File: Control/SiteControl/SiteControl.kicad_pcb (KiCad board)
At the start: 2 copper layers, 109.2 x 48.3 mm, 209 parts, among them J1 RJ50, J2 CONN_01X03, J3 CONN_02X07, J4 CONN_01X06, J5 RS232-Jack, J6 CONN_01X02, J7 USB_A, Q1 BC817-40, Q2 Q_PJFET_GSD, U1 Opto_H11L1M, U10 SS_Relay_VO14642AT, U11 MAX17552, U12 ICL3221, U13 Opto_H11L1M, U14 Opto_H11L1M, U15 12-Bit SPI ADC, U2 Opto_H11L1M, U3 Opto_H11L1M, U4 Opto_H11L1M, U5 Opto_H11L1M, U6 PIC16LF1947, U7 SS_Relay_VO14642AT, U8 SS_Relay_VO14642AT, U9 MC34063, Y1 4MHz

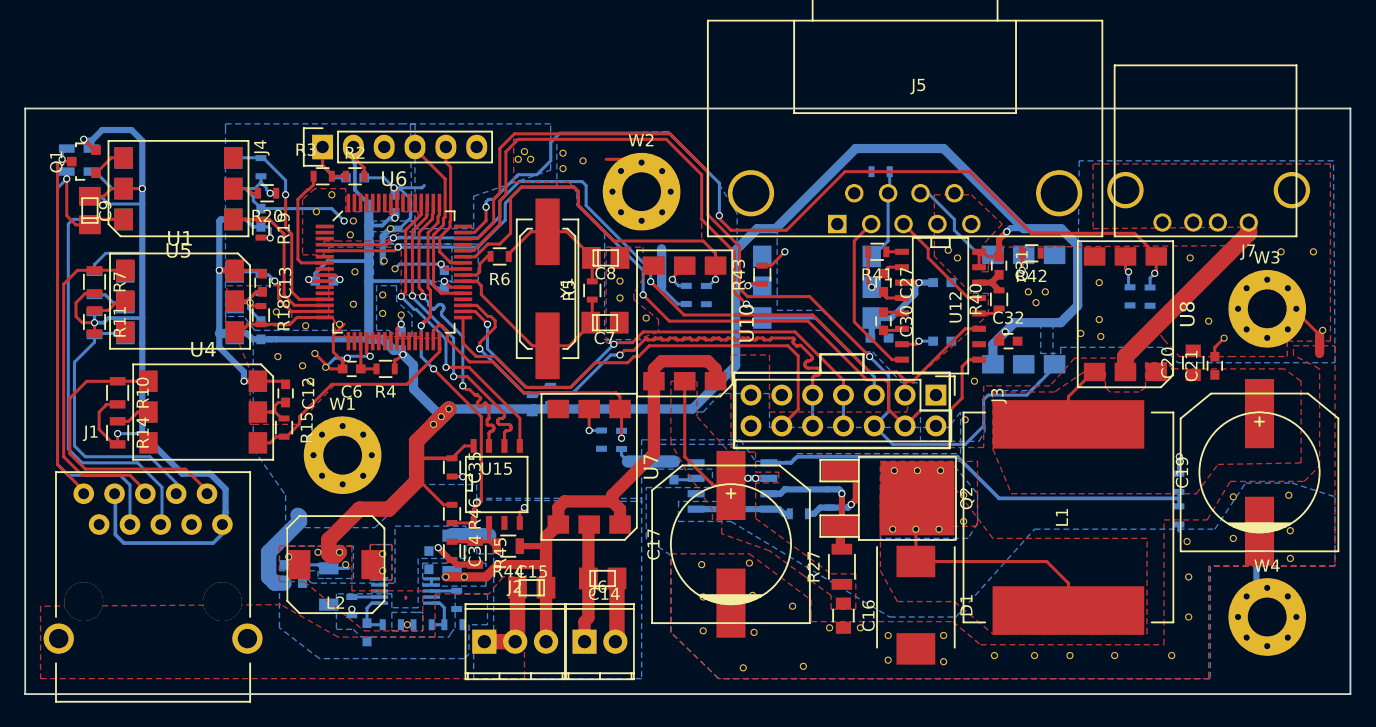
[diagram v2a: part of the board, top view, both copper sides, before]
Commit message: [Changed] Moved the silkscreen identifies as well as added relevant silkscreen text to the board - it should be good to submit to the fab
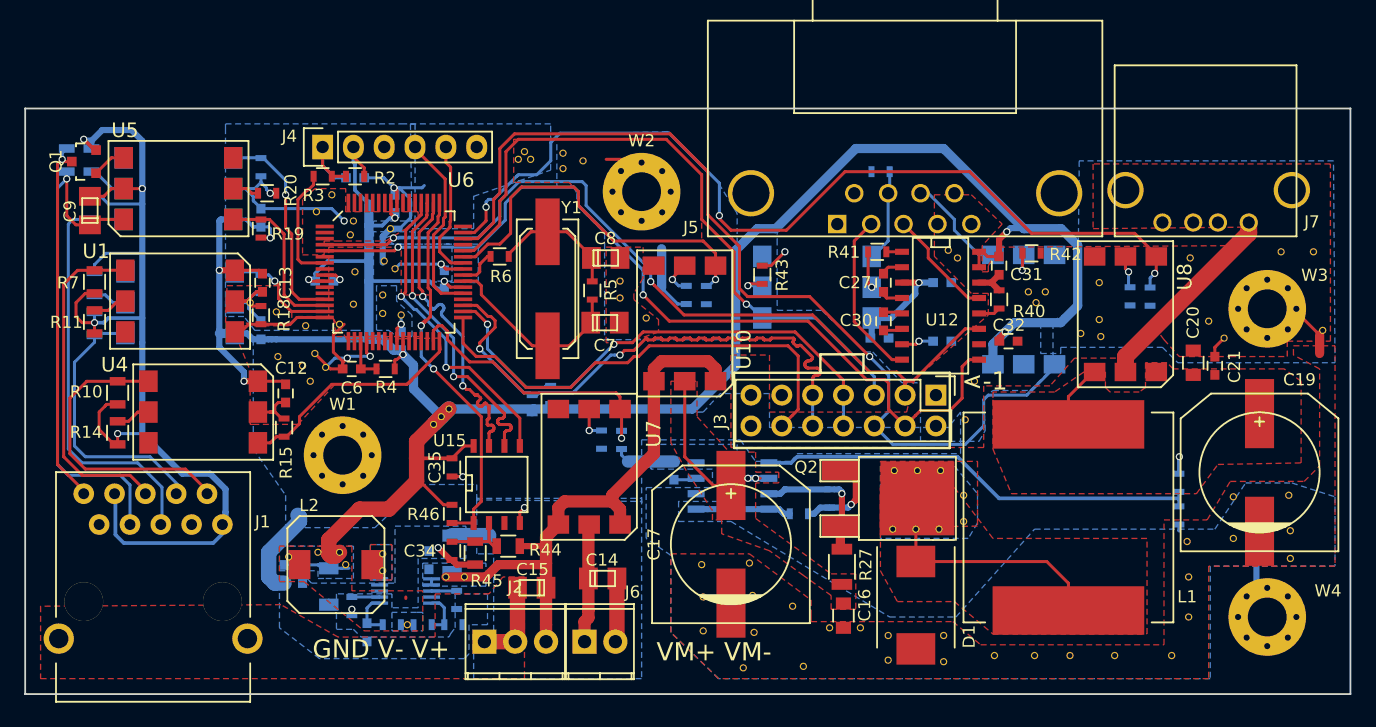
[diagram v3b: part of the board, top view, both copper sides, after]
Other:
- board text added: "<-1"
- board text added: "Applied Physics Club PSU Array Base Control Rev 1.0 The Pennsylvania State University"
- board text added: "GND V- V+"
- board text added: "VM+ VM-"

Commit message: [Added] Site control BOM
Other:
- board text added: "Applied Physics Club PSU Array Site Control Rev 1.0 The Pennsylvania State University"
- board text removed: "Applied Physics Club PSU Array Base Control Rev 1.0 The Pennsylvania State University"
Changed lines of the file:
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@@
     (links 365)
     (no_connects 2)
-    (area 86.284999 63.424999 195.655001 111.835001)
+    (area 85.137535 40.48 214.86 113.305001)
     (thickness 1.6)
     (drawings 19)
@@
     (visible_elements 7FFFFFFF)
     (pcbplotparams
-      (layerselection 0x00030_80000001)
+      (layerselection 0x010f0_80000001)
       (usegerberextensions false)
       (excludeedgelayer true)
@@
       (outputformat 1)
       (mirror false)
-      (drillshape 1)
+      (drillshape 0)
       (scaleselection 1)
       (outputdirectory ""))
@@
     )
   )
-  (gr_text "Applied Physics Club\nPSU Array Base Control Rev 1.0\nThe Pennsylvania State University" (at 163.27 104.17) (layer B.SilkS)
+  (gr_text "Applied Physics Club\nPSU Array Site Control Rev 1.0\nThe Pennsylvania State University" (at 163.27 104.17) (layer B.SilkS)
     (effects (font (size 1.5 1.5) (thickness 0.3)) (justify mirror))
   )
@@
   (gr_line (start 144.78 91.482776) (end 162.56 91.482776) (layer F.SilkS) (width 0.2))
   (dimension 48.26 (width 0.3) (layer Dwgs.User)
-    (gr_text "1.9000 in" (at 208.36 87.63 90) (layer Dwgs.User)
+    (gr_text "48.260 mm" (at 208.36 87.63 90) (layer Dwgs.User)
       (effects (font (size 1.5 1.5) (thickness 0.3)))
     )
@@
     (arrow2b (pts (xy 207.01 111.76) (xy 206.423579 110.633496)))
   )
-  (dimension 109.22 (width 0.3) (layer Dwgs.User)
-    (gr_text "4.3000 in" (at 140.97 41.83) (layer Dwgs.User)
+  (dimension 109.474 (width 0.3) (layer Dwgs.User)
+    (gr_text "109.474 mm" (at 140.839891 41.83) (layer Dwgs.User)
       (effects (font (size 1.5 1.5) (thickness 0.3)))
     )
-    (feature1 (pts (xy 195.58 63.5) (xy 195.58 40.48)))
-    (feature2 (pts (xy 86.36 63.5) (xy 86.36 40.48)))
-    (crossbar (pts (xy 86.36 43.18) (xy 195.58 43.18)))
-    (arrow1a (pts (xy 195.58 43.18) (xy 194.453496 43.766421)))
-    (arrow1b (pts (xy 195.58 43.18) (xy 194.453496 42.593579)))
-    (arrow2a (pts (xy 86.36 43.18) (xy 87.486504 43.766421)))
-    (arrow2b (pts (xy 86.36 43.18) (xy 87.486504 42.593579)))
+    (feature1 (pts (xy 195.576891 63.5) (xy 195.576891 40.48)))
+    (feature2 (pts (xy 86.102891 63.5) (xy 86.102891 40.48)))
+    (crossbar (pts (xy 86.102891 43.18) (xy 195.576891 43.18)))
+    (arrow1a (pts (xy 195.576891 43.18) (xy 194.450387 43.766421)))
+    (arrow1b (pts (xy 195.576891 43.18) (xy 194.450387 42.593579)))
+    (arrow2a (pts (xy 86.102891 43.18) (xy 87.229395 43.766421)))
+    (arrow2b (pts (xy 86.102891 43.18) (xy 87.229395 42.593579)))
   )
   (gr_line (start 86.36 63.5) (end 86.36 111.76) (layer Edge.Cuts) (width 0.15))

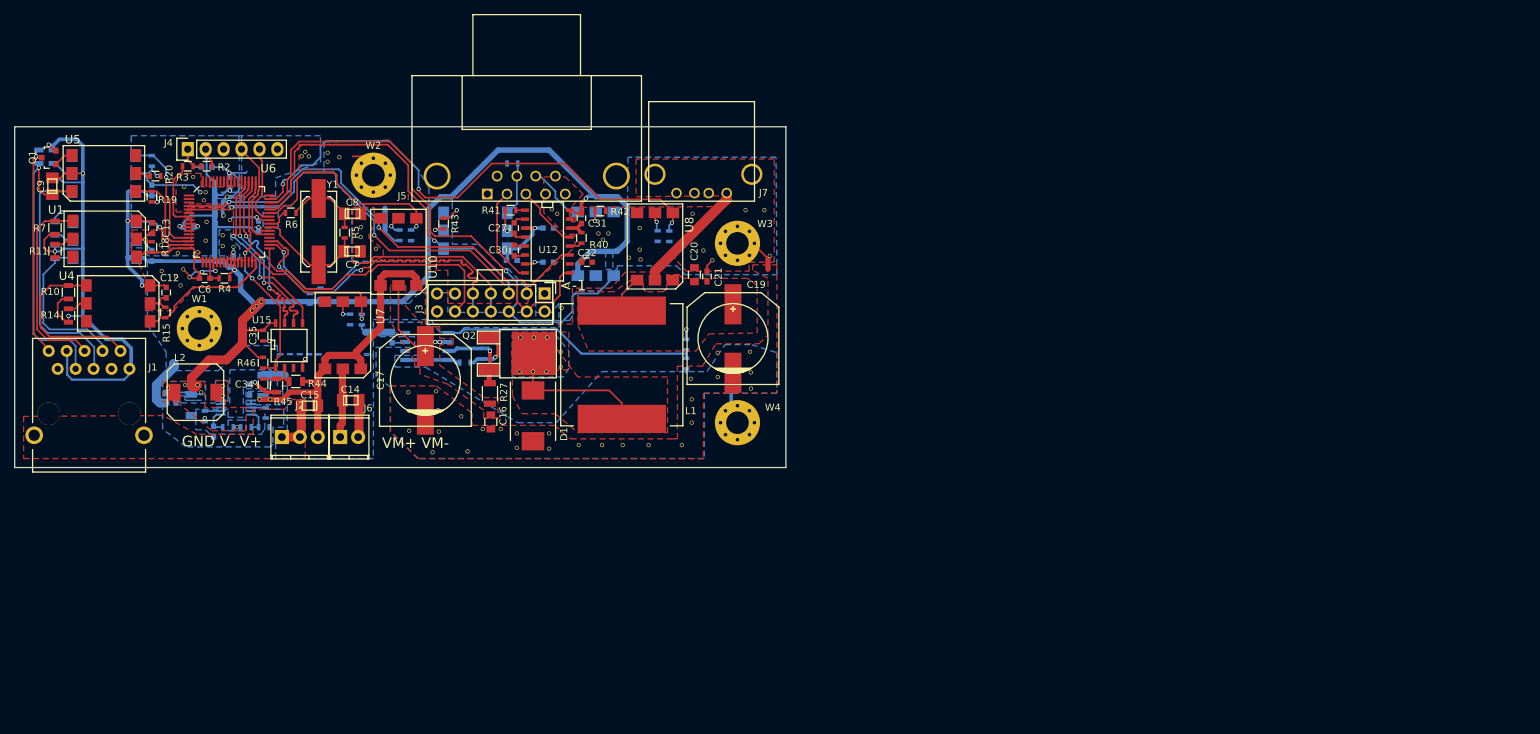
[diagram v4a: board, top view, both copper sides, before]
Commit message: [Added] more parts; [Updated] Site Control board schematic to Rev B; [WIP] Site Control board pcb layout for Rev B.
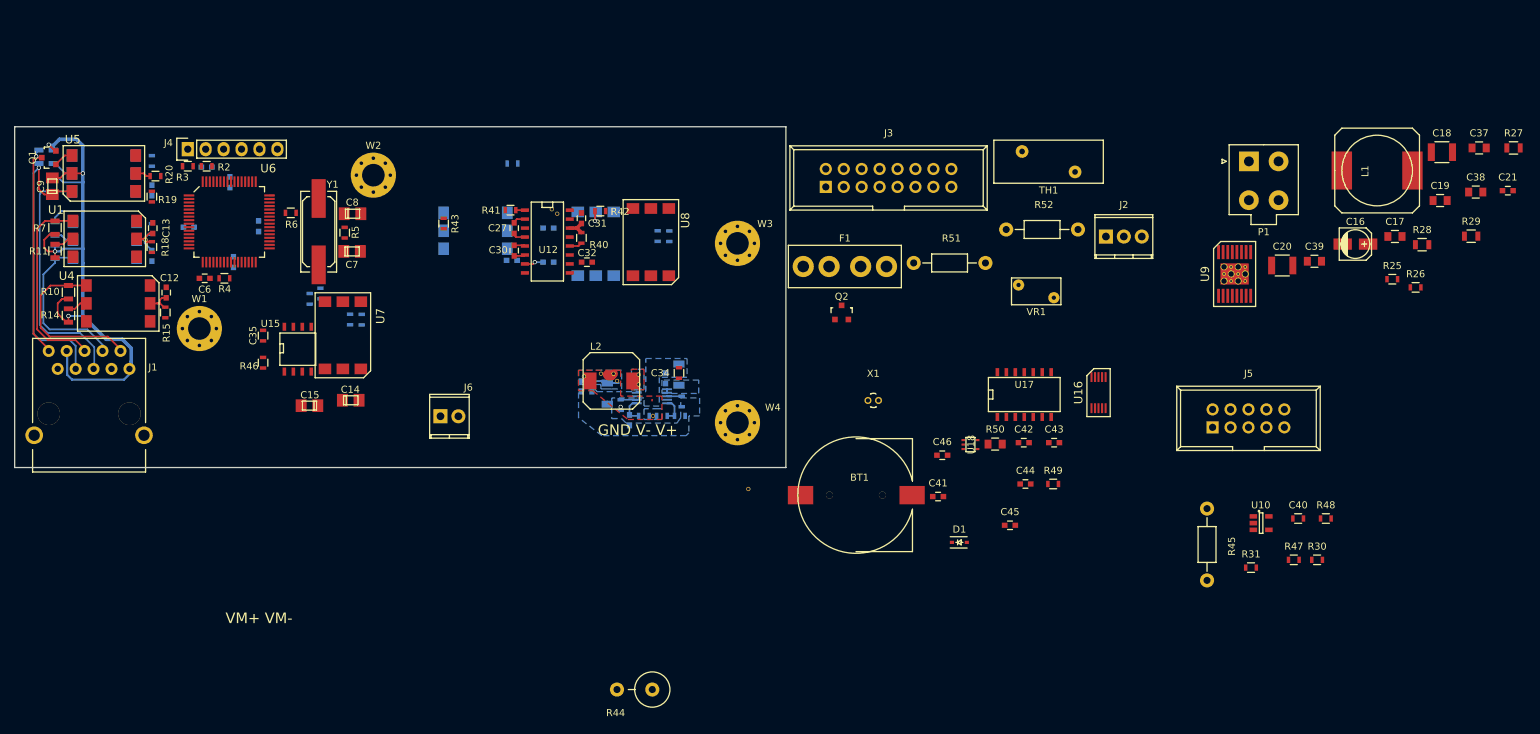
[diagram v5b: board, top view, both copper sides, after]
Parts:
- removed the ? at (107.1, 80.3)
- removed the ? at (175.0, 82.3)
- removed the ? at (174.9, 80.9)
- removed the ? at (173.4, 82.0)
- removed the ? at (169.7, 79.5)
- removed the ? at (170.4, 78.6)
- removed the ? at (169.0, 78.6)
- removed the ? at (164.6, 86.0)
- removed the ? at (163.8, 89.2)
- removed the ? at (137.5, 80.8)
- removed the ? at (135.4, 79.1)
- removed the ? at (135.4, 77.7)
- removed the ? at (132.3, 67.8)
- removed the ? at (130.7, 67.2)
- removed the ? at (130.7, 68.5)
- removed the ? at (128.0, 67.7)
- removed the ? at (127.0, 67.7)
- removed the ? at (127.5, 67.1)
- removed the ? at (110.4, 72.0)
- removed the ? at (193.3, 81.8)
- removed the ? at (111.6, 70.6)
- removed the ? at (116.5, 73.4)
- removed the ? at (113.4, 72.8)
- removed the ? at (113.2, 73.9)
- removed the ? at (115.8, 80.4)
- removed the ? at (115.8, 78.9)
- removed the ? at (116.8, 76.7)
- removed the ? at (116.0, 76.1)
- removed the ? at (113.5, 77.0)
- removed the ? at (192.5, 75.3)
- removed the ? at (113.4, 79.6)
- removed the ? at (112.3, 81.3)
- removed the ? at (109.5, 81.4)
- removed the ? at (110.2, 83.7)
- removed the ? at (107.2, 83.9)
- removed the ? at (109.2, 84.7)
- removed the ? at (111.1, 84.8)
- removed the ? at (109.9, 86.0)
- removed the ? at (120.0, 89.5)
- removed the ? at (120.7, 88.9)
- removed the ? at (189.9, 75.3)
- removed the ? at (121.3, 88.3)
- removed the ? at (149.6, 104.5)
- removed the ? at (145.5, 109.6)
- removed the ? at (150.5, 109.5)
- removed the ? at (190.6, 100.6)
- removed the ? at (190.6, 98.3)
- removed the ? at (190.5, 95.4)
- removed the ? at (185.9, 95.5)
- removed the ? at (185.9, 98.9)
- removed the ? at (182.1, 99.2)
- removed the ? at (185.2, 82.4)
- removed the ? at (182.2, 102.1)
- removed the ? at (182.2, 105.4)
- removed the ? at (180.8, 108.6)
- removed the ? at (176.1, 108.6)
- removed the ? at (172.5, 108.6)
- removed the ? at (169.5, 108.6)
- removed the ? at (166.2, 108.6)
- removed the ? at (157.5, 109.0)
- removed the ? at (162.1, 109.1)
- removed the ? at (162.1, 106.9)
- removed the ? at (183.9, 81.0)
- removed the ? at (157.5, 106.9)
- removed the ? at (155.2, 106.3)
- removed the ? at (152.7, 106.3)
- removed the ? at (146.4, 106.7)
- removed the ? at (142.2, 106.6)
- removed the ? at (142.2, 103.8)
- removed the ? at (146.3, 103.6)
- removed the ? at (146.1, 101.0)
- removed the ? at (142.1, 101.1)
- removed the ? at (159.9, 93.3)
- removed the ? at (182.4, 75.8)
- removed the ? at (158.0, 93.3)
- removed the ? at (161.8, 93.3)
- removed the ? at (163.7, 95.4)
- removed the ? at (163.7, 97.5)
- removed the ? at (161.7, 98.2)
- removed the ? at (159.8, 98.2)
- removed the ? at (157.9, 98.2)
- removed the ? at (122.6, 102.1)
- removed the ? at (121.0, 102.1)
- removed the ? at (174.9, 77.9)
- removed J7: USB_A, Connect:USB_A
- added BT1: Keystone 1056, DigitalLogic:CoinCell_12.5mm, F.Cu at (205.5, 115.7)
- added C37: 0.47uF, Capacitors_SMD:C_0805, F.Cu at (293.8, 66.5)
- added C38: 4.7uF, Capacitors_SMD:C_0805, F.Cu at (293.3, 72.7)
- added C39: 33pF, Capacitors_SMD:C_0805, F.Cu at (270.4, 82.5)
- added C40: 0.1uF, Resistors_SMD:R_0603, F.Cu at (268.1, 119.0)
- added C41: 8pF, Capacitors_SMD:C_0603, F.Cu at (217.1, 115.9)
- added C42: 10pF, Capacitors_SMD:C_0603, F.Cu at (229.3, 108.2)
- added C43: 0.1uF, Capacitors_SMD:C_0603, F.Cu at (233.6, 108.2)
- added C44: 0.1uF, Capacitors_SMD:C_0603, F.Cu at (229.5, 114.1)
- added C45: 0.1uF, Capacitors_SMD:C_0603, F.Cu at (227.3, 119.9)
- added C46: 0.1uF, Capacitors_SMD:C_0603, F.Cu at (217.7, 110.0)
- added F1: BK-6013, DigitalLogic:Mini-Blade_Fuse, F.Cu at (203.9, 83.3)
- added P1: Molex Minifit-JR 4.2mm, Connectors_Molex:Molex_MiniFit-JR-5556-04A_2x02x4.20mm_Straight, F.Cu at (261.1, 68.4)
- added R47: 16K, Resistors_SMD:R_0603, F.Cu at (267.5, 124.8)
- added R48: 39K, Resistors_SMD:R_0603, F.Cu at (272.0, 119.0)
- added R49: 3k, Resistors_SMD:R_0603, F.Cu at (233.4, 114.1)
- added R50: 1R, Capacitors_SMD:C_0805, F.Cu at (225.2, 108.4)
- added R51: 1M, Resistors_ThroughHole:Resistor_Horizontal_RM10mm, F.Cu at (213.7, 82.8)
- added R52: 1M8, Resistors_ThroughHole:Resistor_Horizontal_RM10mm, F.Cu at (226.8, 78.1)
- added TH1: SL15 60004, Varistors:RV_Disc_D15.5_W6.1_P7.5, F.Cu at (229.0, 67.0)
- added U16: MCP7952, DigitalLogic:MSOP-10, F.Cu at (239.9, 101.2)
- added U17: 74HCT125D,653, SMD_Packages:SOIC-14_N, F.Cu at (229.3, 101.3)
- added U18: SN74AUP1T87_Schmitt_XNOR, TO_SOT_Packages_SMD:SOT-353, F.Cu at (221.7, 108.5)
- added VR1: MOV-07D270K, Varistors:RV_Disc_D7_W3.8_P5, F.Cu at (228.5, 85.9)
- added X1: CFS-20632768EZBB_32.768kHz, Crystals:Crystal_Round_Vertical_2mm, F.Cu at (208.0, 102.3)
- C16: value 0.47uF/50V -> 47uF; footprint Capacitors_SMD:C_0805 -> Capacitors_SMD:c_elec_4x5.8
- C17: value 680uF -> 1uF; footprint DigitalLogic:c_elec_13x13 -> Capacitors_SMD:C_0805
- C18: value 1nF -> 22uF; footprint Capacitors_SMD:C_0603 -> Capacitors_SMD:C_1210; moved to F.Cu
- C19: value 1000uF -> 2.2uF; footprint DigitalLogic:c_elec_13x13 -> Capacitors_SMD:C_0805
- C20: value 0.47uF -> 47uF; footprint Capacitors_SMD:C_0805 -> Capacitors_SMD:C_1210
- D1: value ~ -> CUS520,H3F; footprint Diodes_SMD:DO-214AB -> Diodes_SMD:SOD-323
- J3: value CONN_02X07 -> IDC_16Pin_Polarized; footprint Pin_Headers:Pin_Header_Straight_2x07 -> Connect:IDC_Header_Straight_16pins
- J5: value RS232-Jack -> IDC-10_Polarized; footprint Connect:DB9FC -> Connect:IDC_Header_Straight_10pins
- L1: value 100uH -> 22uH; footprint DigitalLogic:SRP1770TA-101M -> Inductors:SELF-WE-PD-XXL
- Q2: value Q_PJFET_GSD -> SI2323DDS-T1-GE3; footprint TO_SOT_Packages_SMD:TO-252-2Lead -> TO_SOT_Packages_SMD:SOT-23
- R25: value 560R -> 10K; moved to F.Cu
- R26: value 10R -> 10K; moved to F.Cu
- R27: value R18 -> 205K; footprint Resistors_SMD:R_1206 -> Resistors_SMD:R_0805
- R28: value 6K8 -> 1M; footprint Resistors_SMD:R_0603 -> Resistors_SMD:R_0805; moved to F.Cu
- R29: value 2K2 -> 255K; footprint Resistors_SMD:R_0603 -> Resistors_SMD:R_0805; moved to F.Cu
- R30: value 10K -> 1M; moved to F.Cu
- R31: value 450R -> 41K; moved to F.Cu
- R44: footprint Resistors_SMD:R_0805 -> Resistors_ThroughHole:Resistor_Vertical_RM5mm
- R45: value 75K -> 20K; footprint Resistors_SMD:R_0805 -> Resistors_ThroughHole:Resistor_Horizontal_RM10mm
- U10: value SS_Relay_VO14642AT -> LMV611; footprint DigitalLogic:SS_Relay_VO14642AT -> TO_SOT_Packages_SMD:SOT-23-5
- U9: value MC34063 -> LM43602; footprint DigitalLogic:MC34063 -> DigitalLogic:TI_HTSSOP-PWP-16; moved to F.Cu
- moved C18 151.0 mm to (288.5, 67.1), turned to 0 degrees
- moved R27 149.1 mm to (298.6, 66.5), turned to 0 degrees
- moved C17 138.8 mm to (281.8, 79.0), turned to 0 degrees
- moved R30 136.3 mm to (270.8, 124.8), turned to 0 degrees
- moved R26 135.1 mm to (284.8, 86.2), turned to 0 degrees
- moved R45 132.9 mm to (255.2, 117.6)
- moved R31 129.5 mm to (261.4, 125.9), turned to 0 degrees
- moved R25 129.2 mm to (281.5, 85.1), turned to 0 degrees
- moved U10 128.1 mm to (262.9, 119.6), turned to 0 degrees
- moved C16 125.0 mm to (276.2, 80.1), turned to 0 degrees
- moved J2 120.1 mm to (240.9, 79.1)
- moved U9 114.9 mm to (259.1, 84.3), turned to 0 degrees
- moved C21 114.1 mm to (297.8, 72.5), turned to 0 degrees
- moved R29 112.6 mm to (292.6, 79.0), turned to 0 degrees
- moved L1 110.4 mm to (279.3, 69.7), turned to 0 degrees
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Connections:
- C16 pad 1: Net-(C16-Pad1) -> +BATT
- C17 pad 1: Net-(C16-Pad1) -> GND
- C17 pad 2: GND -> +BATT
- C18 pad 1: Net-(C18-Pad1) -> GND
- C18 pad 2: GND -> +BATT
- C19 pad 1: +5V -> GND
- C19 pad 2: GND -> Net-(C19-Pad2)
- C28 pad 1: VCC -> +3V3
- C33 pad 1: VCC -> +3V3
- D1 pad 2: GND -> Net-(BT1-Pad1)
- J2 pad 3: +BATT -> Net-(F1-Pad1)
- J3 pad 11: Net-(J3-Pad11) -> PI_SDO
- J3 pad 13: GND -> PI_SDI
- J3 pad 14: GND -> PI_RTC_nCS
- L1 pad 1: Net-(D1-Pad1) -> Net-(C37-Pad2)
- Q2 pad 2: Net-(D1-Pad1) -> +BATT
- R25 pad 1: Net-(Q2-Pad3) -> GND
- R25 pad 2: Net-(Q2-Pad1) -> RPi_5V_En
- R26 pad 1: Net-(Q2-Pad1) -> GND
- R26 pad 2: Net-(R26-Pad2) -> RPi_5v_PGood
- R27 pad 1: Net-(C16-Pad1) -> GND
- R27 pad 2: Net-(Q2-Pad3) -> Net-(R27-Pad2)
- R28 pad 2: Net-(R28-Pad2) -> Net-(C39-Pad1)
- R29 pad 1: Net-(R28-Pad2) -> Net-(C39-Pad1)
- R30 pad 1: GND -> +3V3
- R30 pad 2: RPi_5V_En -> Net-(R30-Pad2)
- R31 pad 1: GND -> Net-(R30-Pad2)
- R31 pad 2: Net-(R31-Pad2) -> GND
- R46 pad 2: ADC_CS -> ADC_nCS
- U10 pad 1: RPi_5V_En -> Net-(C34-Pad1)
- U10 pad 2: Net-(R31-Pad2) -> GND
- U10 pad 3: (no net) -> Net-(R47-Pad1)
- U10 pad 4: +BATT -> Net-(R48-Pad1)
- U10 pad 5: Net-(C16-Pad1) -> +3V3
- U12 pad 3: VCC -> +3V3
- U13 pad 6: VCC -> +3V3
- U15 pad 1: ADC_CS -> ADC_nCS
- U15 pad 2: Net-(C34-Pad1) -> Net-(R48-Pad1)
- U6 pad 48: Net-(U6-Pad48) -> RTC_MFP
- U6 pad 49: ADC_CS -> Net-(U6-Pad49)
- U6 pad 53: Net-(U6-Pad53) -> ADC_nCS
- U6 pad 54: Net-(U6-Pad54) -> RTC_nCS
- U9 pad 1: Net-(R26-Pad2) -> Net-(C37-Pad2)
- U9 pad 2: GND -> Net-(C37-Pad2)
- U9 pad 3: Net-(C18-Pad1) -> Net-(C37-Pad1)
- U9 pad 4: GND -> Net-(C19-Pad2)
- U9 pad 5: Net-(R28-Pad2) -> +5V
- U9 pad 6: Net-(C16-Pad1) -> GND
- U9 pad 7: Net-(Q2-Pad3) -> Net-(R27-Pad2)
- U9 pad 8: Net-(R26-Pad2) -> RPi_5v_PGood
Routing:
- net +3V3: track 221.5 -> 8.07 mm, vias 10 -> 1
- net GND: track 137.6 -> 17.8 mm, vias 13 -> 0
- net CMOS_CTS: track 78.6 -> 0.00 mm, vias 1 -> 0
- net RPi_En: track 75.1 -> 0.00 mm, vias 3 -> 0
- net CMOS_RX: track 72.0 -> 0.00 mm, vias 2 -> 0
- net CMOS_TX: track 69.3 -> 0.00 mm, vias 2 -> 0
- net CMOS_RTS: track 54.6 -> 0.00 mm, vias 1 -> 0
- net +BATT: track 48.6 -> 0.50 mm
- net PiSDA: track 47.0 -> 0.00 mm, vias 2 -> 0
- net PiSCL: track 42.6 -> 0.00 mm, vias 2 -> 0
- net Pi_VSense: track 39.3 -> 0.00 mm
- net Net-(R28-Pad2): track 36.6 -> 0.00 mm
- net ADC_CS: track 31.5 -> 0.00 mm, vias 2 -> 0
- net RPi_5V_En: track 31.0 -> 0.00 mm, vias 1 -> 0
- net SDO: track 26.0 -> 0.00 mm, vias 2 -> 0
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- removed copper zone on F.Cu, net +5V
- removed copper zone on F.Cu, net GND
- removed copper zone on F.Cu, net Net-(C16-Pad1)
- removed copper zone on B.Cu, net Net-(D1-Pad1)
- removed copper zone on F.Cu, net Net-(D1-Pad1)
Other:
- board text removed: "<-1"
